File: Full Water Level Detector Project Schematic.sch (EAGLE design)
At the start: 17 parts, among them IC1 74AHCT125, M1 SMALL_SERVO

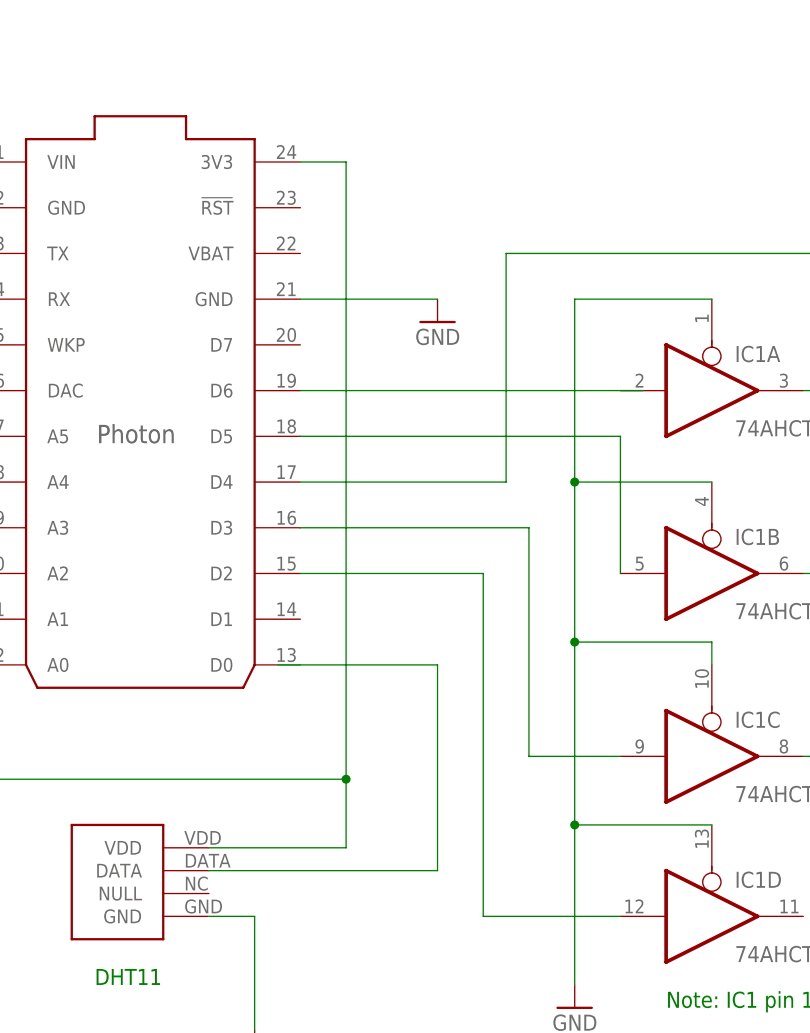
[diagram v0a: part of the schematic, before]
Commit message: Updates schematic
Added pullup resistor required for DHT11.
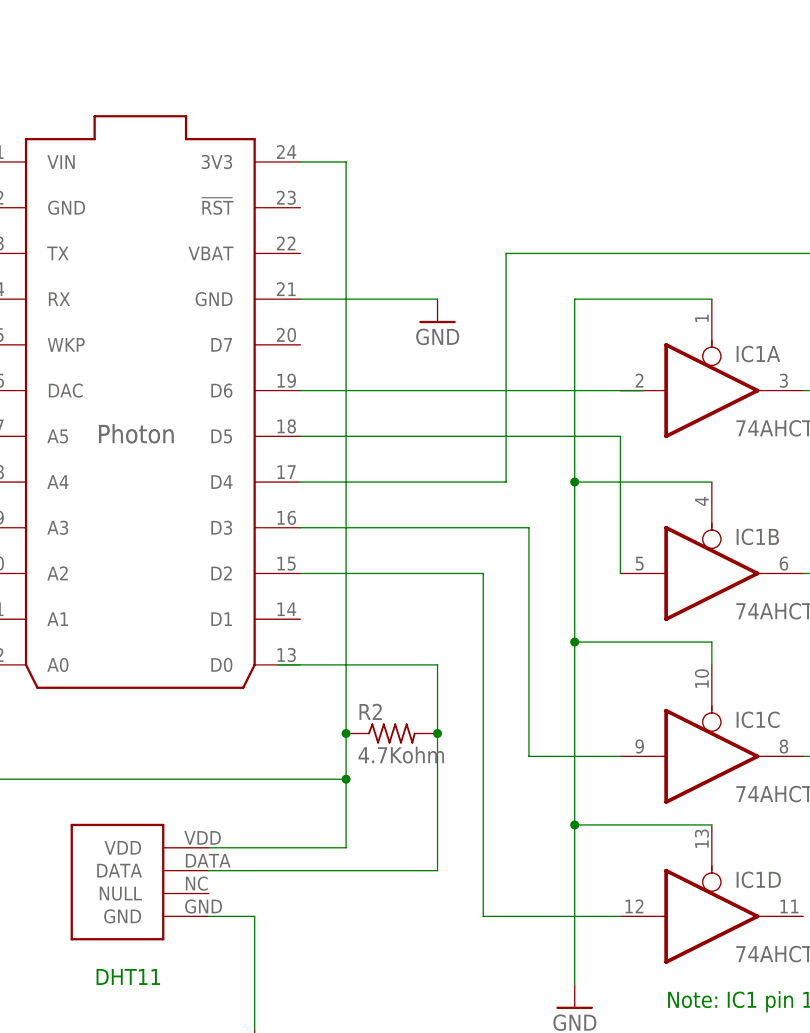
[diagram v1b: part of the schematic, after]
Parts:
- added R2: 4.7Kohm, rcl:R-US_0309/12
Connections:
- net N$19: now also R2.2
- net N$8: now also R2.1
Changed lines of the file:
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@@
 <part name="GND8" library="SparkFun-Aesthetics" deviceset="GND" device=""/>
 <part name="GND9" library="SparkFun-Aesthetics" deviceset="GND" device=""/>
+<part name="R2" library="rcl" deviceset="R-US_" device="0309/12" value="4.7Kohm"/>
 </parts>
 <sheets>
@@
 <instance part="GND8" gate="1" x="93.98" y="55.88" rot="MR0"/>
 <instance part="GND9" gate="1" x="25.4" y="76.2" rot="MR0"/>
+<instance part="R2" gate="G$1" x="20.32" y="30.48"/>
 </instances>
 <busses>
@@
 <pinref part="U$1" gate="G$1" pin="3V3"/>
 <wire x1="10.16" y1="93.98" x2="15.24" y2="93.98" width="0.1524" layer="91"/>
-<wire x1="15.24" y1="93.98" x2="15.24" y2="25.4" width="0.1524" layer="91"/>
+<wire x1="15.24" y1="93.98" x2="15.24" y2="30.48" width="0.1524" layer="91"/>
 <pinref part="U$2" gate="G$1" pin="VDD"/>
+<wire x1="15.24" y1="30.48" x2="15.24" y2="25.4" width="0.1524" layer="91"/>
 <wire x1="15.24" y1="25.4" x2="15.24" y2="17.78" width="0.1524" layer="91"/>
 <wire x1="15.24" y1="17.78" x2="0" y2="17.78" width="0.1524" layer="91"/>
@@
 <junction x="-48.26" y="25.4"/>
 <junction x="15.24" y="25.4"/>
+<pinref part="R2" gate="G$1" pin="1"/>
+<junction x="15.24" y="30.48"/>
 </segment>
 </net>
@@
 <pinref part="U$2" gate="G$1" pin="DATA"/>
 <wire x1="0" y1="15.24" x2="25.4" y2="15.24" width="0.1524" layer="91"/>
-<wire x1="25.4" y1="15.24" x2="25.4" y2="38.1" width="0.1524" layer="91"/>
+<wire x1="25.4" y1="15.24" x2="25.4" y2="30.48" width="0.1524" layer="91"/>
+<wire x1="25.4" y1="30.48" x2="25.4" y2="38.1" width="0.1524" layer="91"/>
 <wire x1="25.4" y1="38.1" x2="7.62" y2="38.1" width="0.1524" layer="91"/>
-</segment>
-</net>
+<pinref part="R2" gate="G$1" pin="2"/>
+<junction x="25.4" y="30.48"/>
+</segment>
+</net>

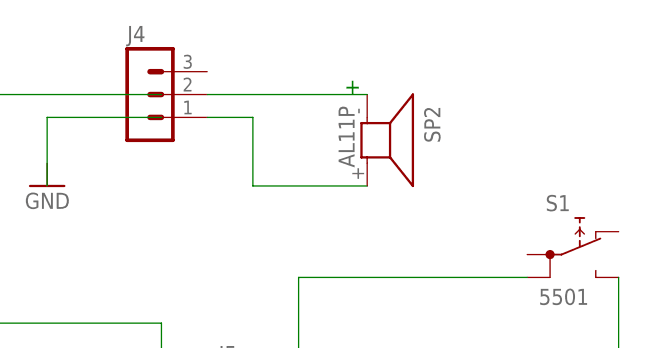
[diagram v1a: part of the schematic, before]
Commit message: Added Piezo Buzzer annotation
Annotated the speaker to indicate that it is a piezo buzzer.
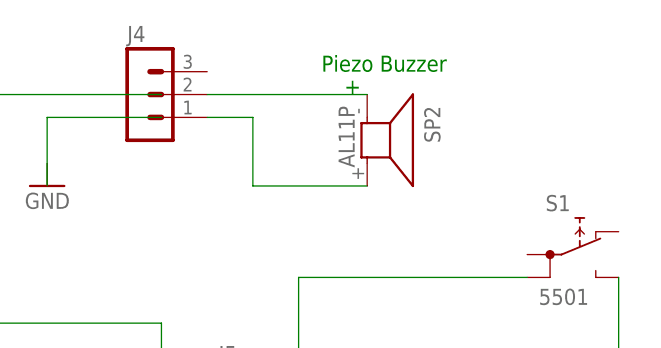
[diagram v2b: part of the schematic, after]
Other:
- note added: "Piezo Buzzer"
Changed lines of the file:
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@@
 <text x="50.8" y="0" size="1.778" layer="91">Note: IC1 pin 14 to Vcc (+5 volts)</text>
 <text x="68.58" y="10.16" size="1.778" layer="91">N/C</text>
+<text x="106.68" y="111.76" size="1.778" layer="91">Piezo Buzzer</text>
 </plain>
 <instances>

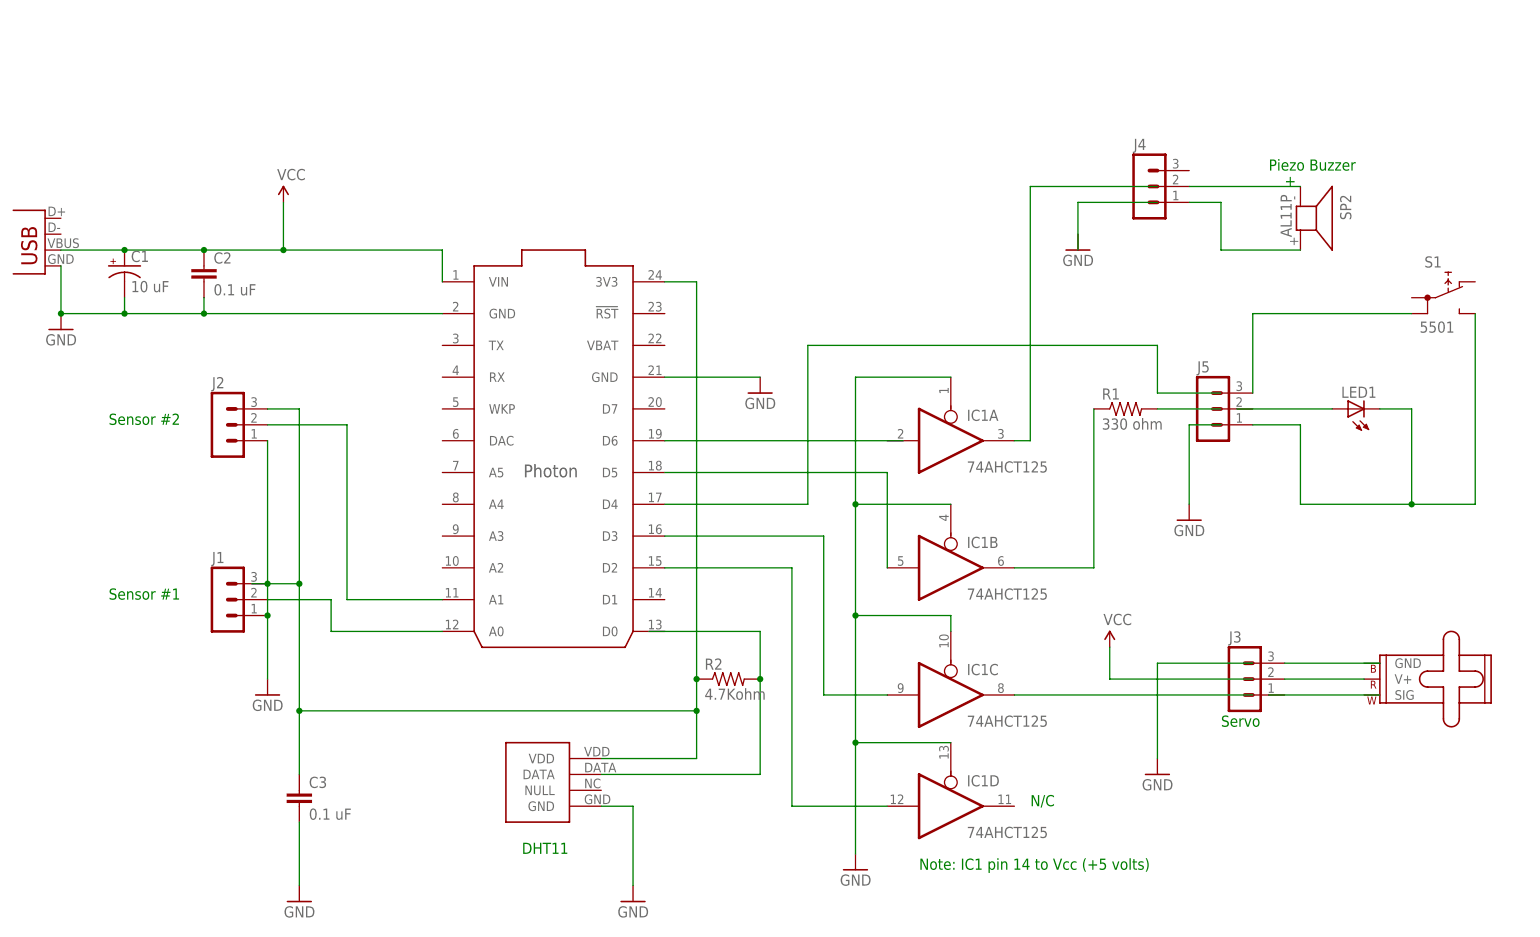
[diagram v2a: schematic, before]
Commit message: Updated schematic
1. added pulldown resistor to piezo buzzer driver input so that buzzer
doesn't sound when flashing/resetting the Photon.
2. added toggle switch.
3. clarified some annotations.
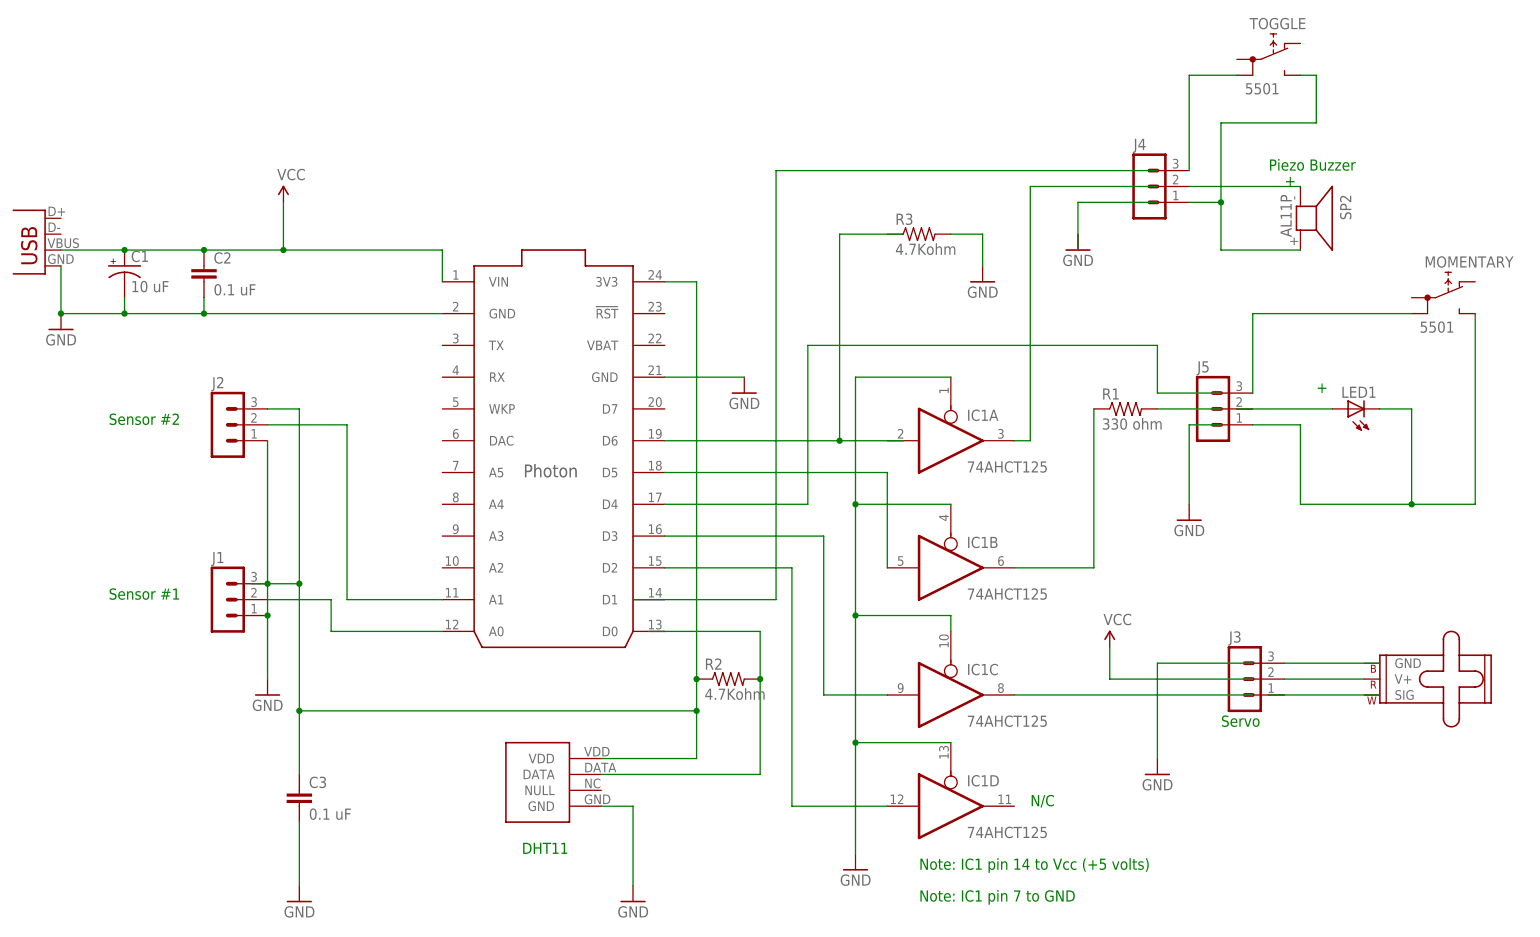
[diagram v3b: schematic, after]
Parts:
- added R3: 4.7Kohm, rcl:R-US_0309/12
- added TOGGLE: 5501, switch:5501
- renumbered S1 to MOMENTARY
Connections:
- new net N$21: J4.3, TOGGLE.1B
- net GND: now also R3.2
- net N$14: now also TOGGLE.NO
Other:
- note added: "Note: IC1 pin 7 to GND"
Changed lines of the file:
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@@
 <part name="GND3" library="SparkFun-Aesthetics" deviceset="GND" device=""/>
 <part name="IC1" library="74xx-us" deviceset="74*125" device="N" value="74AHCT125"/>
-<part name="S1" library="switch" deviceset="55?" device="01"/>
+<part name="MOMENTARY" library="switch" deviceset="55?" device="01"/>
 <part name="R1" library="rcl" deviceset="R-US_" device="0309/12" value="330 ohm"/>
 <part name="LED1" library="led" deviceset="LED" device="5MM"/>
@@
 <part name="GND9" library="SparkFun-Aesthetics" deviceset="GND" device=""/>
 <part name="R2" library="rcl" deviceset="R-US_" device="0309/12" value="4.7Kohm"/>
+<part name="TOGGLE" library="switch" deviceset="55?" device="01"/>
+<part name="R3" library="rcl" deviceset="R-US_" device="0309/12" value="4.7Kohm"/>
+<part name="GND10" library="SparkFun-Aesthetics" deviceset="GND" device=""/>
 </parts>
 <sheets>
@@
 <text x="68.58" y="10.16" size="1.778" layer="91">N/C</text>
 <text x="106.68" y="111.76" size="1.778" layer="91">Piezo Buzzer</text>
+<text x="114.3" y="76.2" size="1.778" layer="91">+</text>
+<text x="50.8" y="-5.08" size="1.778" layer="91">Note: IC1 pin 7 to GND</text>
 </plain>
 <instances>
@@
 <instance part="IC1" gate="C" x="55.88" y="27.94"/>
 <instance part="IC1" gate="D" x="55.88" y="10.16"/>
-<instance part="S1" gate="G$1" x="134.62" y="91.44"/>
+<instance part="MOMENTARY" gate="G$1" x="134.62" y="91.44"/>
 <instance part="R1" gate="G$1" x="83.82" y="73.66"/>
 <instance part="LED1" gate="G$1" x="119.38" y="73.66" rot="R90"/>
@@
 <instance part="GND4" gate="1" x="76.2" y="99.06" rot="MR0"/>
 <instance part="GND8" gate="1" x="93.98" y="55.88" rot="MR0"/>
-<instance part="GND9" gate="1" x="25.4" y="76.2" rot="MR0"/>
+<instance part="GND9" gate="1" x="22.86" y="76.2" rot="MR0"/>
 <instance part="R2" gate="G$1" x="20.32" y="30.48"/>
+<instance part="TOGGLE" gate="G$1" x="106.68" y="129.54"/>
+<instance part="R3" gate="G$1" x="50.8" y="101.6"/>
+<instance part="GND10" gate="1" x="60.96" y="93.98" rot="MR0"/>
 </instances>
 <busses>
@@
 <pinref part="U$1" gate="G$1" pin="GND@21"/>
 <pinref part="GND9" gate="1" pin="GND"/>
-<wire x1="10.16" y1="78.74" x2="25.4" y2="78.74" width="0.1524" layer="91"/>
+<wire x1="10.16" y1="78.74" x2="22.86" y2="78.74" width="0.1524" layer="91"/>
+</segment>
+<segment>
+<pinref part="R3" gate="G$1" pin="2"/>
+<pinref part="GND10" gate="1" pin="GND"/>
+<wire x1="55.88" y1="101.6" x2="60.96" y2="101.6" width="0.1524" layer="91"/>
+<wire x1="60.96" y1="101.6" x2="60.96" y2="96.52" width="0.1524" layer="91"/>
 </segment>
 </net>
@@
 <segment>
 <pinref part="U$1" gate="G$1" pin="D6"/>
-<wire x1="10.16" y1="68.58" x2="48.26" y2="68.58" width="0.1524" layer="91"/>
+<wire x1="10.16" y1="68.58" x2="38.1" y2="68.58" width="0.1524" layer="91"/>
+<wire x1="38.1" y1="68.58" x2="48.26" y2="68.58" width="0.1524" layer="91"/>
+<wire x1="38.1" y1="68.58" x2="38.1" y2="101.6" width="0.1524" layer="91"/>
+<wire x1="38.1" y1="101.6" x2="48.26" y2="101.6" width="0.1524" layer="91"/>
+<junction x="38.1" y="68.58"/>
 </segment>
 </net>
@@
 <pinref part="J5" gate="G$1" pin="1"/>
 <wire x1="111.76" y1="71.12" x2="104.14" y2="71.12" width="0.1524" layer="91"/>
-<pinref part="S1" gate="G$1" pin="NO"/>
+<pinref part="MOMENTARY" gate="G$1" pin="NO"/>
 <wire x1="139.7" y1="88.9" x2="139.7" y2="58.42" width="0.1524" layer="91"/>
 <wire x1="139.7" y1="58.42" x2="129.54" y2="58.42" width="0.1524" layer="91"/>
@@
 <pinref part="SP2" gate="G$1" pin="2"/>
 <wire x1="99.06" y1="99.06" x2="111.76" y2="99.06" width="0.1524" layer="91"/>
+<pinref part="TOGGLE" gate="G$1" pin="NO"/>
+<wire x1="111.76" y1="127" x2="114.3" y2="127" width="0.1524" layer="91"/>
+<wire x1="114.3" y1="127" x2="114.3" y2="119.38" width="0.1524" layer="91"/>
+<wire x1="114.3" y1="119.38" x2="99.06" y2="119.38" width="0.1524" layer="91"/>
+<wire x1="99.06" y1="119.38" x2="99.06" y2="106.68" width="0.1524" layer="91"/>
+<junction x="99.06" y="106.68"/>
 </segment>
 </net>
@@
 <segment>
 <pinref part="J5" gate="G$1" pin="3"/>
-<pinref part="S1" gate="G$1" pin="1B"/>
+<pinref part="MOMENTARY" gate="G$1" pin="1B"/>
 <wire x1="104.14" y1="88.9" x2="129.54" y2="88.9" width="0.1524" layer="91"/>
 <wire x1="104.14" y1="88.9" x2="104.14" y2="76.2" width="0.1524" layer="91"/>
 </segment>
 </net>
+<net name="N$21" class="0">
+<segment>
+<pinref part="J4" gate="G$1" pin="3"/>
+<wire x1="93.98" y1="111.76" x2="93.98" y2="127" width="0.1524" layer="91"/>
+<pinref part="TOGGLE" gate="G$1" pin="1B"/>
+<wire x1="93.98" y1="127" x2="101.6" y2="127" width="0.1524" layer="91"/>
+</segment>
+</net>
+<net name="N$23" class="0">
+<segment>
+<wire x1="88.9" y1="111.76" x2="27.94" y2="111.76" width="0.1524" layer="91"/>
+<wire x1="27.94" y1="111.76" x2="27.94" y2="43.18" width="0.1524" layer="91"/>
+<wire x1="27.94" y1="43.18" x2="5.08" y2="43.18" width="0.1524" layer="91"/>
+</segment>
+</net>
